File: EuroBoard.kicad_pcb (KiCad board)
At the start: 2 copper layers, 99.9 x 99.9 mm, 36 parts, among them J1 GPIO, J10 PD1, J11 PD2, J12 PD3, J2 Conn_01x07_Male, J3 I2C, J4 Conn_01x05_Male, J5 RX, J6 TX, J7 GND, SW1 RESET, SW2 SW_DIP_x04, U1 AMS1117-3.3, U2 STM32G030CxT, Y1 NX2520 16MHz

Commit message: Rework
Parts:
- removed C11: 10u, Capacitor_SMD:C_0805_2012Metric_Pad1.18x1.45mm_HandSolder
- removed J1: GPIO, Connector_PinHeader_2.54mm:PinHeader_1x08_P2.54mm_Vertical
- removed J10: PD1, TestPoint:TestPoint_Pad_1.0x1.0mm
- removed J11: PD2, TestPoint:TestPoint_Pad_1.0x1.0mm
- removed J12: PD3, TestPoint:TestPoint_Pad_1.0x1.0mm
- removed J2: Conn_01x07_Male, Connector_PinHeader_2.54mm:PinHeader_1x07_P2.54mm_Vertical
- removed J3: I2C, Connector_PinHeader_2.54mm:PinHeader_1x03_P2.54mm_Vertical
- removed J4: Conn_01x05_Male, Connector_PinHeader_2.54mm:PinHeader_1x05_P2.54mm_Vertical
- removed J5: RX, TestPoint:TestPoint_Pad_1.0x1.0mm
- removed J6: TX, TestPoint:TestPoint_Pad_1.0x1.0mm
- removed J7: GND, TestPoint:TestPoint_Pad_1.0x1.0mm
- removed REF**: ProtoArea, MEMS_Custom:ProtoArea
- added C5: 8p, Capacitor_SMD:C_0805_2012Metric_Pad1.18x1.45mm_HandSolder, F.Cu at (187.8, 97.4)
- added R3: 10k, Capacitor_SMD:C_0805_2012Metric_Pad1.18x1.45mm_HandSolder, F.Cu at (192.8, 119.1)
- added R4: 0R, Capacitor_SMD:C_0805_2012Metric_Pad1.18x1.45mm_HandSolder, F.Cu at (186.8, 94.4)
- added R5: 1k, Resistor_SMD:R_0805_2012Metric_Pad1.20x1.40mm_HandSolder, F.Cu at (185.8, 58.0)
- added TP1: SPI1_SCK, MEMS_Custom:TestPoint_Pad_D1.0mm, F.Cu at (180.9, 83.8)
- added TP10: GP0, MEMS_Custom:TestPoint_Pad_D1.0mm, F.Cu at (171.7, 88.7)
- added TP11: GND, MEMS_Custom:TestPoint_Pad_D1.0mm, F.Cu at (168.2, 100.6)
- added TP12: GND, MEMS_Custom:TestPoint_Pad_D1.0mm, F.Cu at (187.2, 101.9)
- added TP13: GND, MEMS_Custom:TestPoint_Pad_D1.0mm, F.Cu at (171.0, 62.3)
- added TP14: GND, MEMS_Custom:TestPoint_Pad_D1.0mm, F.Cu at (170.2, 85.3)
- added TP15: GND, MEMS_Custom:TestPoint_Pad_D1.0mm, F.Cu at (185.3, 85.3)
- added TP16: 3V3, MEMS_Custom:TestPoint_Pad_D1.0mm, F.Cu at (174.5, 62.3)
- added TP2: SPI1_MISO, MEMS_Custom:TestPoint_Pad_D1.0mm, F.Cu at (178.9, 83.8)
- added TP3: SPI1_MOSI, MEMS_Custom:TestPoint_Pad_D1.0mm, F.Cu at (176.8, 83.9)
- added TP4: SCL_INT, MEMS_Custom:TestPoint_Pad_D1.0mm, F.Cu at (168.3, 94.7)
- added TP5: SDA_INT, MEMS_Custom:TestPoint_Pad_D1.0mm, F.Cu at (168.3, 97.0)
- added TP6: TRG, MEMS_Custom:TestPoint_Pad_D1.0mm, F.Cu at (192.8, 103.8)
- added TP7: RDY, MEMS_Custom:TestPoint_Pad_D1.0mm, F.Cu at (184.1, 101.9)
- added TP8: GP2, MEMS_Custom:TestPoint_Pad_D1.0mm, F.Cu at (174.1, 85.9)
- added TP9: GP1, MEMS_Custom:TestPoint_Pad_D1.0mm, F.Cu at (172.2, 86.7)
- C1: value C -> 8p
- C12: moved to F.Cu
- C2, D2, L1: moved to B.Cu
- C7: value C -> 100n; moved to B.Cu
- C8: value 100n -> 10u
- R1: value R -> 0R; footprint Resistor_SMD:R_0805_2012Metric_Pad1.20x1.40mm_HandSolder -> Capacitor_SMD:C_0805_2012Metric_Pad1.18x1.45mm_HandSolder
- R2: value 1k -> 0R; footprint Resistor_SMD:R_0805_2012Metric_Pad1.20x1.40mm_HandSolder -> Capacitor_SMD:C_0805_2012Metric_Pad1.18x1.45mm_HandSolder
- moved C12 106.5 mm to (187.6, 128.4), turned to 90 degrees
- moved C15 63.8 mm to (187.6, 75.2), turned to 90 degrees
- moved C14 63.1 mm to (187.6, 71.2), turned to 90 degrees
- moved C13 62.5 mm to (187.6, 67.2), turned to -90 degrees
- moved R2 62.1 mm to (186.8, 91.4)
- moved C1 60.1 mm to (184.8, 99.8), turned to 0 degrees
- moved Y1 56.2 mm to (185.2, 97.2), turned to 180 degrees
- moved C2 51.7 mm to (191.0, 85.4), turned to 180 degrees
- moved R1 51.3 mm to (186.8, 89.3), turned to 180 degrees
- moved L1 51.0 mm to (181.4, 90.6), turned to 0 degrees
- moved C8 50.9 mm to (181.4, 92.6), turned to 180 degrees
- moved D2 50.1 mm to (191.2, 87.8), turned to 180 degrees
- moved C7 50.0 mm to (181.4, 94.6), turned to 180 degrees
- moved SW2 49.9 mm to (174.0, 103.2), turned to -90 degrees
- moved U2 46.2 mm to (178.2, 92.4), turned to 180 degrees
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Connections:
- B1 pad 11: /SCL -> /SCL_EXT
- B1 pad 13: /SDA -> /SDA_EXT
- C1 pad 1: /OSC_IN -> Net-(U2-Pad2)
- C4 pad 1: Net-(C4-Pad1) -> +3.3V
- C6 pad 1: Net-(C4-Pad1) -> +3.3V
- C7 pad 1: Net-(C7-Pad1) -> Net-(U2-Pad5)
- C8 pad 1: /VREF -> Net-(L1-Pad2)
- L1 pad 1: Net-(C4-Pad1) -> +3.3V
- L1 pad 2: +3.3V -> Net-(L1-Pad2)
- R1 pad 1: Net-(C7-Pad1) -> /SCL_EXT
- R1 pad 2: /OSC_OUT -> /SCL_INT
- R2 pad 1: Net-(D1-Pad2) -> /SDA_INT
- R2 pad 2: /LED -> /SDA_EXT
- SW2 pad 1: Net-(SW2-Pad1) -> Net-(U2-Pad41)
- SW2 pad 2: Net-(SW2-Pad2) -> Net-(U2-Pad40)
- SW2 pad 3: Net-(SW2-Pad3) -> Net-(U2-Pad39)
- SW2 pad 4: Net-(SW2-Pad4) -> Net-(U2-Pad38)
- U1 pad 2: Net-(C4-Pad1) -> +3.3V
- U2 pad 1: /LED -> /PC13
- U2 pad 11: Net-(J1-Pad1) -> /PA0
- U2 pad 12: /SPI1_SCK -> /PA1
- U2 pad 15: Net-(J1-Pad5) -> /PA4
- U2 pad 16: Net-(J1-Pad6) -> /SPI1_SCK
- U2 pad 19: /TRG -> /PB0
- U2 pad 2: unconnected-(U2-Pad2) -> Net-(U2-Pad2)
- U2 pad 20: /RDY -> /PB1
- U2 pad 21: /GP2 -> /PB2
- U2 pad 22: /SCL2 -> /GP2
- U2 pad 23: /SDA2 -> /GP1
- U2 pad 24: Net-(SW2-Pad4) -> /GP0
- U2 pad 25: Net-(SW2-Pad3) -> /SPI2_SCK
- U2 pad 26: Net-(SW2-Pad2) -> /SPI2_MISO
- U2 pad 27: Net-(SW2-Pad1) -> /SPI2_MOSI
- U2 pad 28: unconnected-(U2-Pad28) -> /PA8
- U2 pad 29: /TX_AUX -> /PA9
- U2 pad 3: unconnected-(U2-Pad3) -> Net-(U2-Pad3)
- U2 pad 30: unconnected-(U2-Pad30) -> /PB6
- U2 pad 31: unconnected-(U2-Pad31) -> Net-(U2-Pad31)
- U2 pad 32: /RX_AUX -> /PA10
- U2 pad 33: /GP0 -> /SCL_INT
- U2 pad 34: /GP1 -> /SDA_INT
- U2 pad 37: unconnected-(U2-Pad37) -> /PA15
- U2 pad 38: unconnected-(U2-Pad38) -> Net-(U2-Pad38)
- U2 pad 4: +3.3V -> Net-(L1-Pad2)
- U2 pad 40: Net-(J11-Pad1) -> Net-(U2-Pad40)
- U2 pad 41: Net-(J12-Pad1) -> Net-(U2-Pad41)
- U2 pad 42: Net-(J2-Pad1) -> /PB3
- U2 pad 43: Net-(J2-Pad2) -> /PB4
- U2 pad 44: Net-(J2-Pad3) -> /PB5
- U2 pad 45: /SCL -> /SCL_EXT
- U2 pad 46: /SDA -> /SDA_EXT
- U2 pad 47: Net-(J2-Pad6) -> /TRG
- U2 pad 48: Net-(J2-Pad7) -> /RDY
- U2 pad 5: /VREF -> Net-(U2-Pad5)
- U2 pad 6: +3.3V -> Net-(L1-Pad2)
- U2 pad 8: /OSC_IN -> /PF0
- U2 pad 9: /OSC_OUT -> /PF1
- Y1 pad 1: Net-(C7-Pad1) -> Net-(Y1-Pad1)
- Y1 pad 3: /OSC_IN -> Net-(U2-Pad2)
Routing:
- net +5V: track 70.5 -> 8.04 mm, vias 1 -> 0
- net Net-(U2-Pad31): track 0.00 -> 60.9 mm, vias 0 -> 2
- net /SCL: track 59.6 -> 0.00 mm, vias 1 -> 0
- net /SDA: track 58.4 -> 0.00 mm, vias 1 -> 0
- net GND: track 12.1 -> 59.0 mm, vias 25 -> 19
- net +3.3V: track 141.7 -> 95.4 mm, vias 2 -> 5
- net /SPI1_MOSI: track 45.2 -> 5.02 mm, vias 1 -> 0
- net +12V: track 44.9 -> 5.17 mm
- net Net-(J1-Pad6): track 37.9 -> 0.00 mm, vias 1 -> 0
- net -12V: track 42.8 -> 5.19 mm
- net /SPI1_MISO: track 41.6 -> 4.42 mm, vias 1 -> 0
- net Net-(J1-Pad5): track 33.8 -> 0.00 mm, vias 1 -> 0
- net /SDA_INT: track 0.00 -> 29.5 mm, vias 0 -> 2
- net /SCL_INT: track 0.00 -> 29.0 mm, vias 0 -> 2
- net /TX_DEBUG: track 88.2 -> 59.5 mm
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- added copper zone on F.Cu, net +3.3V
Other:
- board text removed: "-12V"
- board text removed: "12V"
- board text removed: "3.3V"
- board text removed: "5V"
- board text removed: "EuroMeasure Evaluation Module v1.0"
- board text removed: "GND"
- board text removed: "Michał Zychla 2023"
- board text removed: "SCL"
- board text removed: "SDA"

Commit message: Added jumpers for address selection
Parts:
- added JP1: ADR0, MEMS_Passive:R_0805_2012Metric_Jumper, F.Cu at (172.0, 101.8)
- added JP2: ADR1, MEMS_Passive:R_0805_2012Metric_Jumper, F.Cu at (175.0, 101.8)
- added JP3: ADR2, MEMS_Passive:R_0805_2012Metric_Jumper, F.Cu at (177.0, 101.8)
- added JP4: ADR3, MEMS_Passive:R_0805_2012Metric_Jumper, F.Cu at (179.0, 101.8)
- SW2: value SW_DIP_x04 -> ADR
- moved SW2 2.91 mm to (176.7, 102.2)
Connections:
- net Net-(U2-Pad38) renamed /ADR0
- net Net-(U2-Pad39) renamed /ADR1
- net Net-(U2-Pad40) renamed /ADR2
- net Net-(U2-Pad41) renamed /ADR3
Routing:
- net /SWCLK: track 59.4 -> 61.4 mm
- net /SWDIO: track 49.8 -> 51.5 mm
- net /ADR3: track 4.20 -> 5.29 mm
- net /ADR1: track 6.01 -> 4.98 mm
- net GND: vias 19 -> 20

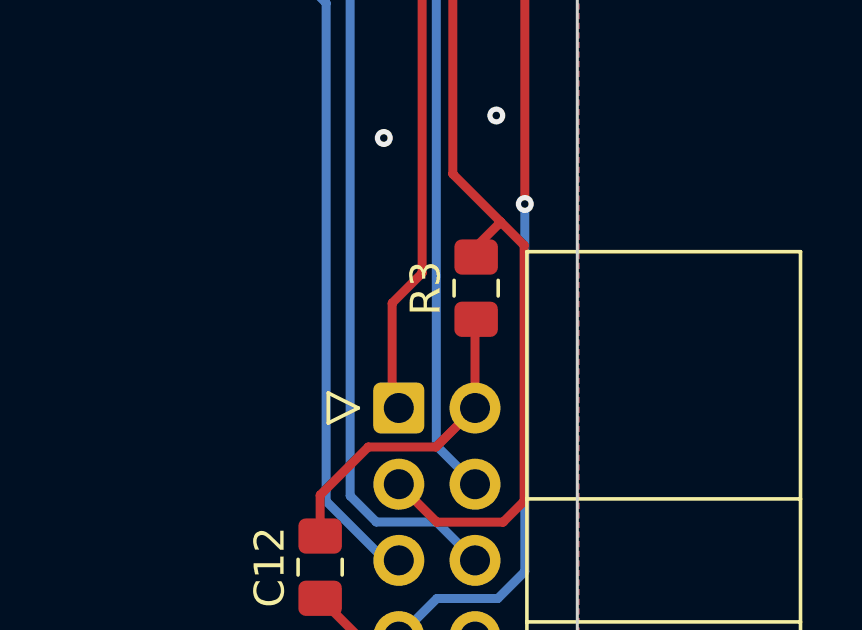
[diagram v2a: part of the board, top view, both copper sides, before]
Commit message: removed R3 from pcb
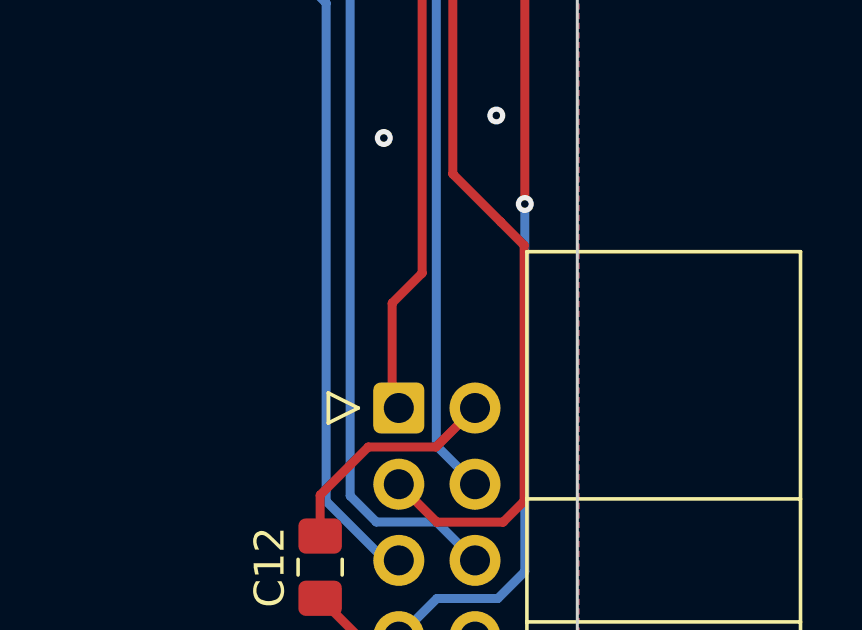
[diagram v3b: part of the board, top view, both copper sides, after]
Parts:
- removed R3: 10k, Capacitor_SMD:C_0805_2012Metric_Pad1.18x1.45mm_HandSolder
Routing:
- net GND: track 59.0 -> 56.0 mm
- net /SWCLK: track 61.4 -> 59.9 mm
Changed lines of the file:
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@@
-    )
-  )
-  (footprint "Capacitor_SMD:C_0805_2012Metric_Pad1.18x1.45mm_HandSolder" (layer "F.Cu")
-    (at 192.8 119.1 90)
-    (descr "Capacitor SMD 0805 (2012 Metric), square (rectangular) end terminal, IPC_7351 nominal with elongated pad for handsoldering. (Body size source: IPC-SM-782 page 76, https://www.pcb-3d.com/wordpress/wp-content/uploads/ipc-sm-782a_amendment_1_and_2.pdf, https://docs.google.com/spreadsheets/d/1BsfQQcO9C6DZCsRaXUlFlo91Tg2WpOkGARC1WS5S8t0/edit?usp=sharing), generated with kicad-footprint-generator")
-    (tags "capacitor handsolder")
-    (property "Sheetfile" "EuroBoard.kicad_sch")
-    (property "Sheetname" "")
-    (attr smd)
-    (fp_text reference "R3" (at 0 -1.68 90) (layer "F.SilkS")
-      (effects (font (size 1 1) (thickness 0.15)))
-    )
-    (fp_text value "10k" (at 0 1.68 90) (layer "F.Fab")
-      (effects (font (size 1 1) (thickness 0.15)))
-    )
-    (fp_text user "${REFERENCE}" (at 0 0 90) (layer "F.Fab")
-      (effects (font (size 0.5 0.5) (thickness 0.08)))
-    )
-    (fp_line (start -0.261252 -0.735) (end 0.261252 -0.735) (layer "F.SilkS") (width 0.12))
-    (fp_line (start -0.261252 0.735) (end 0.261252 0.735) (layer "F.SilkS") (width 0.12))
-    (fp_line (start 1.88 0.98) (end -1.88 0.98) (layer "F.CrtYd") (width 0.05))
-    (fp_line (start -1.88 -0.98) (end 1.88 -0.98) (layer "F.CrtYd") (width 0.05))
-    (fp_line (start 1.88 -0.98) (end 1.88 0.98) (layer "F.CrtYd") (width 0.05))
-    (fp_line (start -1.88 0.98) (end -1.88 -0.98) (layer "F.CrtYd") (width 0.05))
-    (fp_line (start -1 -0.625) (end 1 -0.625) (layer "F.Fab") (width 0.1))
-    (fp_line (start -1 0.625) (end -1 -0.625) (layer "F.Fab") (width 0.1))
-    (fp_line (start 1 -0.625) (end 1 0.625) (layer "F.Fab") (width 0.1))
-    (fp_line (start 1 0.625) (end -1 0.625) (layer "F.Fab") (width 0.1))
-    (pad "1" smd roundrect (at -1.0375 0 90) (size 1.175 1.45) (layers "F.Cu" "F.Paste" "F.Mask") (roundrect_rratio 0.212766)
-      (net 2 "GND") (pintype "passive"))
-    (pad "2" smd roundrect (at 1.0375 0 90) (size 1.175 1.45) (layers "F.Cu" "F.Paste" "F.Mask") (roundrect_rratio 0.212766)
-      (net 12 "/SWCLK") (pintype "passive"))
-    (model "${KICAD6_3DMODEL_DIR}/Capacitor_SMD.3dshapes/C_0805_2012Metric.wrl"
-      (offset (xyz 0 0 0))
-      (scale (xyz 1 1 1))
-      (rotate (xyz 0 0 0))
     )
   )
@@
   (segment (start 180.2375 76.4125) (end 182.35 74.3) (width 1) (layer "F.Cu") (net 2))
   (segment (start 180.2375 76.8) (end 180.2375 76.4125) (width 1) (layer "F.Cu") (net 2))
-  (segment (start 192.7625 120.175) (end 192.8 120.1375) (width 0.3) (layer "F.Cu") (net 2))
-  (segment (start 192.7625 123.095) (end 192.7625 120.175) (width 0.3) (layer "F.Cu") (net 2))
   (segment (start 187.8 99.2) (end 187.8 98.4375) (width 0.3) (layer "F.Cu") (net 2))
   (segment (start 191.4625 124.395) (end 192.7625 123.095) (width 0.3) (layer "F.Cu") (net 2))
@@
   (segment (start 174.0375 95.15) (end 173.05 95.15) (width 0.3) (layer "F.Cu") (net 12))
   (segment (start 191.4875 126.9) (end 190.2225 125.635) (width 0.3) (layer "F.Cu") (net 12))
-  (segment (start 192.8 117.7175) (end 193.6225 116.895) (width 0.3) (layer "F.Cu") (net 12))
   (segment (start 169.9725 98.2275) (end 169.9725 103.095) (width 0.3) (layer "F.Cu") (net 12))
   (segment (start 193.7 126.9) (end 191.4875 126.9) (width 0.3) (layer "F.Cu") (net 12))
   (segment (start 173.05 95.15) (end 169.9725 98.2275) (width 0.3) (layer "F.Cu") (net 12))
-  (segment (start 192.8 118.0625) (end 192.8 117.7175) (width 0.3) (layer "F.Cu") (net 12))
   (segment (start 173.4725 106.595) (end 179.4725 106.595) (width 0.3) (layer "F.Cu") (net 12))
   (segment (start 190.1275 105.4) (end 192.0225 107.295) (width 0.3) (layer "F.Cu") (net 12))

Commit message: Fixed pin numbering error
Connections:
- net /PB6 renamed /PC6

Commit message: Changed bus voltage from 12V to 15V
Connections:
- net +12V renamed +15V
- net -12V renamed -15V
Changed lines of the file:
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@@
   )
   (net 0 "")
-  (net 1 "-12V")
+  (net 1 "-15V")
   (net 2 "GND")
   (net 3 "+5V")
-  (net 4 "+12V")
+  (net 4 "+15V")
   (net 5 "/GP2")
   (net 6 "/RST")
@@
     (fp_line (start 93.68 46.4) (end 98.38 46.4) (layer "F.Fab") (width 0.1))
     (pad "1" thru_hole roundrect locked (at 94 16) (size 1.7 1.7) (drill 1) (layers *.Mask "F.Cu" "In1.Cu" "B.Cu") (roundrect_rratio 0.1470588235)
-      (net 1 "-12V") (pinfunction "-12V") (pintype "bidirectional"))
+      (net 1 "-15V") (pinfunction "-15V") (pintype "power_out"))
     (pad "2" thru_hole circle locked (at 96.54 16) (size 1.7 1.7) (drill 1) (layers *.Mask "F.Cu" "In1.Cu" "B.Cu")
-      (net 1 "-12V") (pinfunction "-12V") (pintype "bidirectional"))
+      (net 1 "-15V") (pinfunction "-15V") (pintype "passive"))
     (pad "3" thru_hole circle locked (at 95 5) (size 5.6 5.6) (drill 3.2) (layers *.Cu *.Mask)
-      (net 2 "GND") (pinfunction "GND") (pintype "bidirectional"))
+      (net 2 "GND") (pinfunction "GND") (pintype "power_out"))
     (pad "3" thru_hole circle locked (at 94 18.54) (size 1.7 1.7) (drill 1) (layers *.Mask "F.Cu" "In1.Cu" "B.Cu")
-      (net 2 "GND") (pinfunction "GND") (pintype "bidirectional"))
+      (net 2 "GND") (pinfunction "GND") (pintype "power_out"))
     (pad "3" thru_hole circle locked (at 5 5) (size 5.6 5.6) (drill 3.2) (layers *.Cu *.Mask)
-      (net 2 "GND") (pinfunction "GND") (pintype "bidirectional"))
+      (net 2 "GND") (pinfunction "GND") (pintype "power_out"))
     (pad "3" thru_hole circle locked (at 5 95) (size 5.6 5.6) (drill 3.2) (layers *.Cu *.Mask)
-      (net 2 "GND") (pinfunction "GND") (pintype "bidirectional"))
+      (net 2 "GND") (pinfunction "GND") (pintype "power_out"))
     (pad "3" thru_hole circle locked (at 95 95) (size 5.6 5.6) (drill 3.2) (layers *.Cu *.Mask)
-      (net 2 "GND") (pinfunction "GND") (pintype "bidirectional"))
+      (net 2 "GND") (pinfunction "GND") (pintype "power_out"))
     (pad "4" thru_hole circle locked (at 96.54 18.54) (size 1.7 1.7) (drill 1) (layers *.Mask "F.Cu" "In1.Cu" "B.Cu")
-      (net 2 "GND") (pinfunction "GND") (pintype "bidirectional"))
+      (net 2 "GND") (pinfunction "GND") (pintype "passive"))
     (pad "5" thru_hole circle locked (at 94 21.08) (size 1.7 1.7) (drill 1) (layers *.Mask "F.Cu" "In1.Cu" "B.Cu")
-      (net 3 "+5V") (pinfunction "5V") (pintype "bidirectional"))
+      (net 3 "+5V") (pinfunction "5V") (pintype "power_out"))
     (pad "6" thru_hole circle locked (at 96.54 21.08) (size 1.7 1.7) (drill 1) (layers *.Mask "F.Cu" "In1.Cu" "B.Cu")
-      (net 3 "+5V") (pinfunction "5V") (pintype "bidirectional"))
+      (net 3 "+5V") (pinfunction "5V") (pintype "passive"))
     (pad "7" thru_hole circle locked (at 94 23.62) (size 1.7 1.7) (drill 1) (layers *.Mask "F.Cu" "In1.Cu" "B.Cu")
-      (net 2 "GND") (pinfunction "GND") (pintype "bidirectional"))
+      (net 2 "GND") (pinfunction "GND") (pintype "passive"))
     (pad "8" thru_hole circle locked (at 96.54 23.62) (size 1.7 1.7) (drill 1) (layers *.Mask "F.Cu" "In1.Cu" "B.Cu")
-      (net 2 "GND") (pinfunction "GND") (pintype "bidirectional"))
+      (net 2 "GND") (pinfunction "GND") (pintype "passive"))
     (pad "9" thru_hole circle locked (at 94 26.16) (size 1.7 1.7) (drill 1) (layers *.Mask "F.Cu" "In1.Cu" "B.Cu")
-      (net 4 "+12V") (pinfunction "12V") (pintype "bidirectional"))
+      (net 4 "+15V") (pinfunction "15V") (pintype "power_out"))
     (pad "10" thru_hole circle locked (at 96.54 26.16) (size 1.7 1.7) (drill 1) (layers *.Mask "F.Cu" "In1.Cu" "B.Cu")
-      (net 4 "+12V") (pinfunction "12V") (pintype "bidirectional"))
+      (net 4 "+15V") (pinfunction "15V") (pintype "passive"))
     (pad "11" thru_hole roundrect locked (at 94 41) (size 1.7 1.7) (drill 1) (layers *.Cu *.Mask) (roundrect_rratio 0.1470588235)
       (net 25 "/SCL_EXT") (pinfunction "SCL") (pintype "bidirectional"))
     (pad "12" thru_hole circle locked (at 96.54 41) (size 1.7 1.7) (drill 1) (layers *.Cu *.Mask)
-      (net 2 "GND") (pinfunction "GND") (pintype "bidirectional"))
+      (net 2 "GND") (pinfunction "GND") (pintype "passive"))
     (pad "13" thru_hole circle locked (at 94 43.54) (size 1.7 1.7) (drill 1) (layers *.Cu *.Mask)
       (net 26 "/SDA_EXT") (pinfunction "SDA") (pintype "bidirectional"))
     (pad "14" thru_hole circle locked (at 96.54 43.54) (size 1.7 1.7) (drill 1) (layers *.Cu *.Mask)
-      (net 2 "GND") (pinfunction "GND") (pintype "bidirectional"))
+      (net 2 "GND") (pinfunction "GND") (pintype "passive"))
     (pad "15" thru_hole circle locked (at 94 46.08) (size 1.7 1.7) (drill 1) (layers *.Cu *.Mask)
-      (net 5 "/GP2") (pinfunction "NC4") (pintype "bidirectional"))
+      (net 5 "/GP2") (pinfunction "GP2") (pintype "bidirectional"))
     (pad "16" thru_hole circle locked (at 96.54 46.08) (size 1.7 1.7) (drill 1) (layers *.Cu *.Mask)
       (net 6 "/RST") (pinfunction "RST") (pintype "bidirectional"))
     (pad "17" thru_hole circle locked (at 94 48.62) (size 1.7 1.7) (drill 1) (layers *.Cu *.Mask)
-      (net 7 "/GP0") (pinfunction "NC2") (pintype "bidirectional"))
+      (net 7 "/GP0") (pinfunction "GP0") (pintype "bidirectional"))
     (pad "18" thru_hole circle locked (at 96.54 48.62) (size 1.7 1.7) (drill 1) (layers *.Cu *.Mask)
-      (net 8 "/GP1") (pinfunction "NC3") (pintype "bidirectional"))
+      (net 8 "/GP1") (pinfunction "GP1") (pintype "bidirectional"))
     (pad "19" thru_hole circle locked (at 94 51.16) (size 1.7 1.7) (drill 1) (layers *.Cu *.Mask)
       (net 9 "/TRG") (pinfunction "TRG") (pintype "bidirectional"))
@@
       (net 11 "/SWDIO") (pinfunction "SWDIO") (pintype "bidirectional"))
     (pad "22" thru_hole circle locked (at 96.54 73) (size 1.7 1.7) (drill 1) (layers *.Cu *.Mask)
-      (net 2 "GND") (pinfunction "GND") (pintype "bidirectional"))
+      (net 2 "GND") (pinfunction "GND") (pintype "power_in"))
     (pad "23" thru_hole circle locked (at 94 75.54) (size 1.7 1.7) (drill 1) (layers *.Cu *.Mask)
       (net 12 "/SWCLK") (pinfunction "SWCLK") (pintype "bidirectional"))
@@
       (net 14 "/TX_DEBUG") (pinfunction "TX") (pintype "bidirectional"))
     (pad "27" thru_hole circle locked (at 94 80.62) (size 1.7 1.7) (drill 1) (layers *.Cu *.Mask)
-      (net 15 "+3.3V") (pinfunction "3.3V") (pintype "bidirectional"))
+      (net 15 "+3.3V") (pinfunction "3.3V") (pintype "power_in"))
     (pad "28" thru_hole circle locked (at 96.54 80.62) (size 1.7 1.7) (drill 1) (layers *.Cu *.Mask)
-      (net 16 "unconnected-(B1-Pad28)") (pinfunction "NC4") (pintype "bidirectional"))
+      (net 16 "unconnected-(B1-Pad28)") (pinfunction "NC4") (pintype "bidirectional+no_connect"))
     (pad "29" thru_hole circle locked (at 94 83.16) (size 1.7 1.7) (drill 1) (layers *.Cu *.Mask)
-      (net 17 "unconnected-(B1-Pad29)") (pinfunction "NC5") (pintype "bidirectional"))
+      (net 17 "unconnected-(B1-Pad29)") (pinfunction "NC5") (pintype "bidirectional+no_connect"))
     (pad "30" thru_hole circle locked (at 96.54 83.16) (size 1.7 1.7) (drill 1) (layers *.Cu *.Mask)
-      (net 18 "unconnected-(B1-Pad30)") (pinfunction "NC6") (pintype "bidirectional"))
+      (net 18 "unconnected-(B1-Pad30)") (pinfunction "NC6") (pintype "bidirectional+no_connect"))
   )
   (footprint "Capacitor_SMD:C_0805_2012Metric_Pad1.18x1.45mm_HandSolder" (layer "F.Cu")
@@
     (fp_line (start -1 -0.625) (end -1 0.625) (layer "B.Fab") (width 0.1))
     (pad "1" smd roundrect (at -1.0375 0 90) (size 1.175 1.45) (layers "B.Cu" "B.Paste" "B.Mask") (roundrect_rratio 0.212766)
-      (net 4 "+12V") (pintype "passive"))
+      (net 4 "+15V") (pintype "passive"))
     (pad "2" smd roundrect (at 1.0375 0 90) (size 1.175 1.45) (layers "B.Cu" "B.Paste" "B.Mask") (roundrect_rratio 0.212766)
       (net 2 "GND") (pintype "passive"))
@@
     (fp_line (start -1 -0.625) (end -1 0.625) (layer "B.Fab") (width 0.1))
     (pad "1" smd roundrect (at -1.0375 0 270) (size 1.175 1.45) (layers "B.Cu" "B.Paste" "B.Mask") (roundrect_rratio 0.212766)
-      (net 1 "-12V") (pintype "passive"))
+      (net 1 "-15V") (pintype "passive"))
     (pad "2" smd roundrect (at 1.0375 0 270) (size 1.175 1.45) (layers "B.Cu" "B.Paste" "B.Mask") (roundrect_rratio 0.212766)
       (net 2 "GND") (pintype "passive"))
